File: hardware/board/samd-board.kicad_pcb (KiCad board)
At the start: 2 copper layers, 20.3 x 40.6 mm, 23 parts, among them J1 USB_B_Mini, J2 Conn_ARM_JTAG_SWD_10, J3 Conn_01x16_Male, J4 Conn_01x16_Male, SW1 SW_Push, U1 AZ1117-3.3, U2 ATSAMD21E17D-A, Y1 8MHz

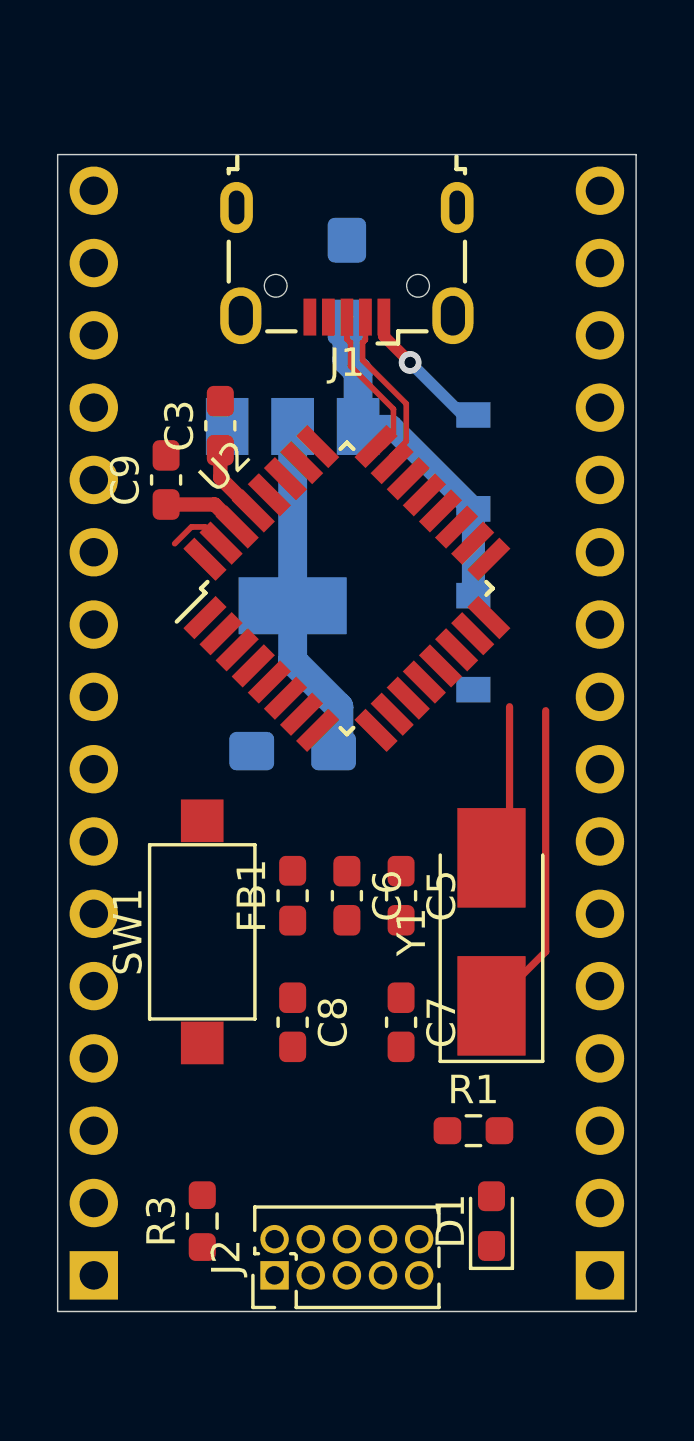
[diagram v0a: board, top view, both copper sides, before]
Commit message: complete basic routing
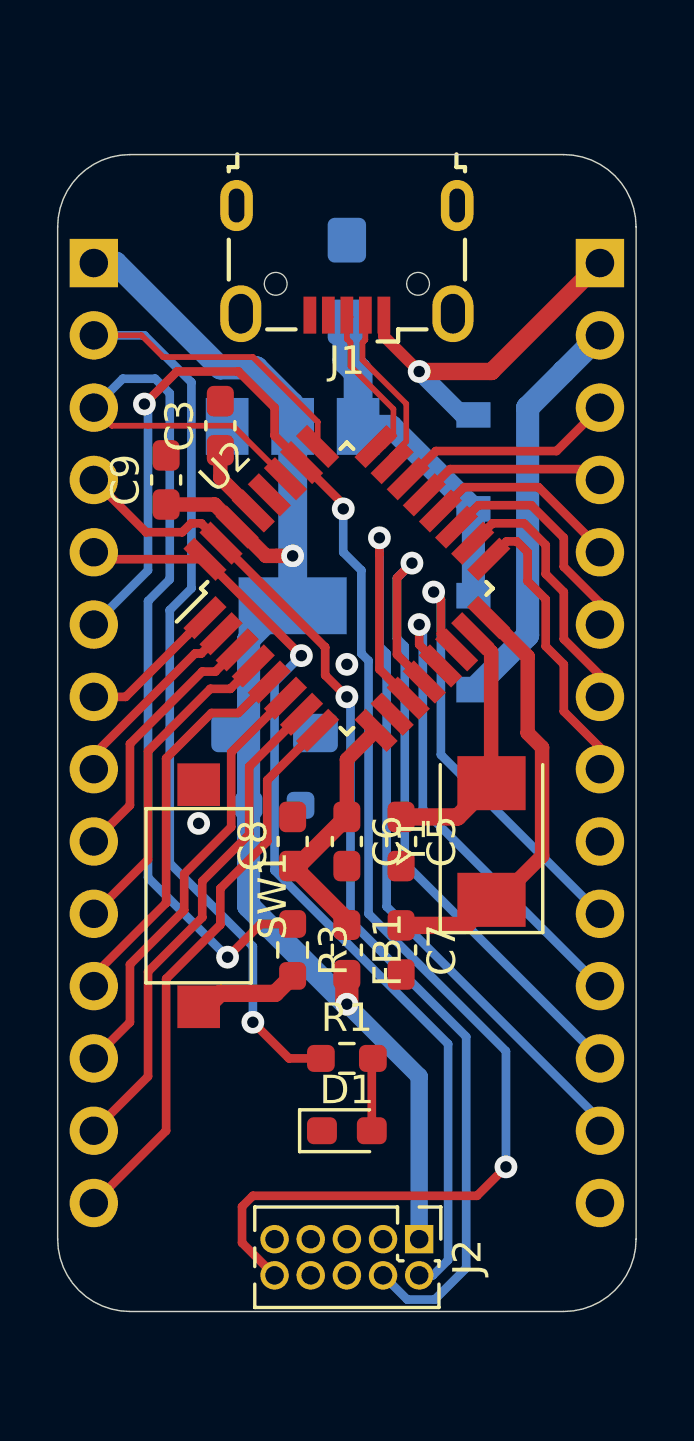
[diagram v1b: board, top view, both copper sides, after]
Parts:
- removed J3, J4: Conn_01x16_Male, Connector_PinHeader_2.54mm:PinHeader_1x16_P2.54mm_Vertical
- added J5: Conn_01x14_Male, Connector_PinHeader_2.54mm:PinHeader_1x14_P2.54mm_Vertical, B.Cu at (181.6, 83.8)
- added J6: Conn_01x14_Male, Connector_PinHeader_2.54mm:PinHeader_1x14_P2.54mm_Vertical, B.Cu at (199.4, 83.8)
- added R2: NP, Resistor_SMD:R_0603_1608Metric_Pad0.98x0.95mm_HandSolder, B.Cu at (188.0, 102.9)
- J1: footprint Connector_USB:USB_Micro-B_Wuerth_629105150521 -> Assorted:USB_Micro-B_Wuerth_629105150521
- Y1: footprint Crystal:Crystal_SMD_5032-2Pin_5.0x3.2mm_HandSoldering -> Assorted:Crystal_SMD_Abracon_ABM3-2Pin_5.0x3.2mm
- moved R3 10.0 mm to (188.6, 108.0), turned to 270 degrees
- moved C8 6.35 mm to (188.6, 104.1), turned to 90 degrees
- moved D1 5.99 mm to (190.5, 114.3), turned to 0 degrees
- moved J2 5.24 mm to (193.0, 118.1), turned to 270 degrees
- moved R1 5.12 mm to (190.5, 111.8)
- moved J1 3.82 mm to (190.5, 80.0)
- moved Y1 3.17 mm to (195.6, 104.1)
- moved FB1 2.69 mm to (190.5, 108.0), turned to 270 degrees
- moved C7 2.54 mm to (192.4, 108.0)
- moved C5 1.91 mm to (192.4, 104.1)
- moved C6 1.91 mm to (190.5, 104.1)
- moved SW1 1.28 mm to (185.3, 106.0), turned to 270 degrees
- moved C4 0.90 mm to (188.0, 100.3), turned to 0 degrees
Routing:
- net ~RESET: track 0.00 -> 56.9 mm, vias 0 -> 3
- net /PA27: track 0.00 -> 41.0 mm, vias 0 -> 1
- net SWCLK: track 2.81 -> 38.4 mm, vias 0 -> 1
- net /PA28: track 0.00 -> 34.7 mm, vias 0 -> 1
- net +3V3: track 14.9 -> 49.3 mm, vias 0 -> 2
- net SWDIO: track 0.00 -> 34.2 mm, vias 0 -> 1
- net /PA08: track 0.00 -> 30.1 mm, vias 0 -> 1
- net /PA09: track 0.00 -> 25.4 mm, vias 0 -> 1
- net /PA07: track 0.00 -> 19.9 mm
- net /PA06: track 0.00 -> 17.7 mm
- net /PA10: track 0.00 -> 17.1 mm, vias 0 -> 1
- net /PA11: track 0.00 -> 16.1 mm, vias 0 -> 1
- net /PA05: track 0.00 -> 15.4 mm
- net VDC: track 0.00 -> 14.3 mm
- net /PA04: track 0.00 -> 13.8 mm
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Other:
- outline, holes or cut-outs redrawn

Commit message: increase pin count from 28 to 32, complete routing
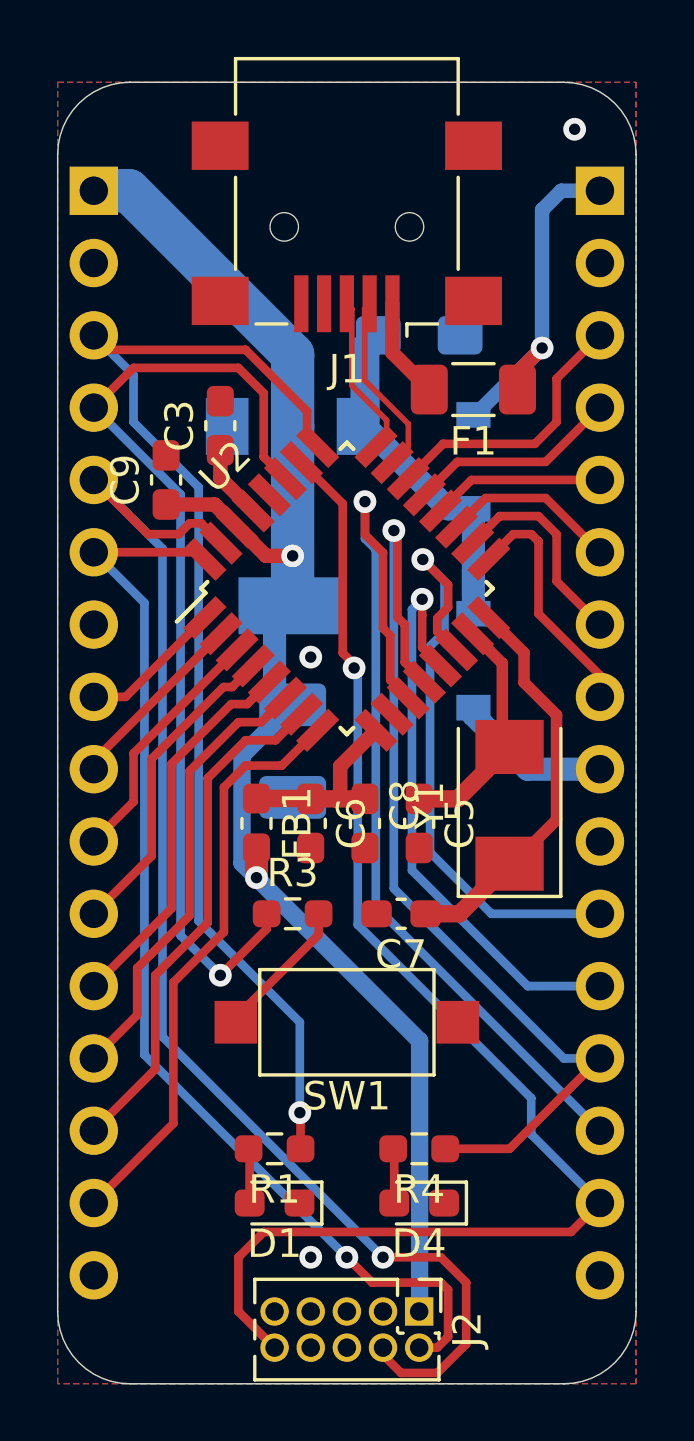
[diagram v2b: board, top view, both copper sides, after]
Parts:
- removed J5, J6: Conn_01x14_Male, Connector_PinHeader_2.54mm:PinHeader_1x14_P2.54mm_Vertical
- removed R2: NP, Resistor_SMD:R_0603_1608Metric_Pad0.98x0.95mm_HandSolder
- added D4: LED, LED_SMD:LED_0603_1608Metric_Pad1.05x0.95mm_HandSolder, F.Cu at (193.0, 116.8)
- added F1: Polyfuse, Resistor_SMD:R_1206_3216Metric_Pad1.30x1.75mm_HandSolder, F.Cu at (194.9, 88.3)
- added J3: Conn_01x16_Male, Connector_PinHeader_2.54mm:PinHeader_1x16_P2.54mm_Vertical, B.Cu at (181.6, 81.3)
- added J4: Conn_01x16_Male, Connector_PinHeader_2.54mm:PinHeader_1x16_P2.54mm_Vertical, B.Cu at (199.4, 81.3)
- added R4: 1k5, Resistor_SMD:R_0603_1608Metric_Pad0.98x0.95mm_HandSolder, F.Cu at (193.0, 114.9)
- C4: footprint Capacitor_Tantalum_SMD:CP_EIA-3216-18_Kemet-A_Pad1.58x1.35mm_HandSolder -> Capacitor_Tantalum_SMD:CP_EIA-3528-21_Kemet-B_Pad1.50x2.35mm_HandSolder
- J1: footprint Assorted:USB_Micro-B_Wuerth_629105150521 -> Connector_USB:USB_Mini-B_Lumberg_2486_01_Horizontal
- moved SW1 6.85 mm to (190.5, 110.5), turned to 180 degrees
- moved FB1 5.46 mm to (187.3, 103.5)
- moved R1 4.07 mm to (188.0, 114.9), turned to 180 degrees
- moved D1 3.59 mm to (188.0, 116.8), turned to 180 degrees
- moved C2 3.17 mm to (193.0, 86.4), turned to 0 degrees
- moved C8 2.62 mm to (191.1, 103.5), turned to 270 degrees
- moved J1 2.55 mm to (190.5, 82.5)
- moved J2 2.54 mm to (193.0, 120.7)
- moved C6 1.42 mm to (189.2, 103.5)
- moved Y1 1.42 mm to (196.2, 102.9)
- moved C7 1.27 mm to (192.4, 106.7), turned to 180 degrees
- moved R3 1.27 mm to (188.6, 106.7), turned to 0 degrees
- moved C4 0.90 mm to (188.6, 101.0), turned to 270 degrees
- moved C5 0.90 mm to (193.0, 103.5)
- moved D2 0.64 mm to (194.9, 97.8)
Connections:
- J1 pad 1: VBUS -> Net-(F1-Pad2)
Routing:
- net /PA09: track 25.4 -> 34.8 mm
- net ~RESET: track 56.9 -> 47.5 mm, vias 3 -> 1
- net VDC: track 14.3 -> 5.49 mm
- net SWCLK: track 38.4 -> 46.5 mm
- net /PA11: track 16.1 -> 21.7 mm
- net SWDIO: track 34.2 -> 39.3 mm
- net +3V3: track 49.3 -> 53.5 mm
- net Net-(F1-Pad2): track 0.00 -> 3.55 mm
- net /PA10: track 17.1 -> 20.6 mm
- net /PA08: track 30.1 -> 33.0 mm
- net +3.3VA: track 8.95 -> 6.82 mm
- net /PA23: track 7.77 -> 9.71 mm
- net Net-(D4-Pad2): track 0.00 -> 1.92 mm
- net /PA17: track 9.29 -> 7.41 mm
- net /PA18: track 8.13 -> 6.25 mm
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- added copper zone on B.Cu, net GND
- added copper zone on F.Cu, net GND
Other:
- board size 20.3 x 40.6 mm -> 20.3 x 45.7 mm

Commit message: complete component silkscreen placement
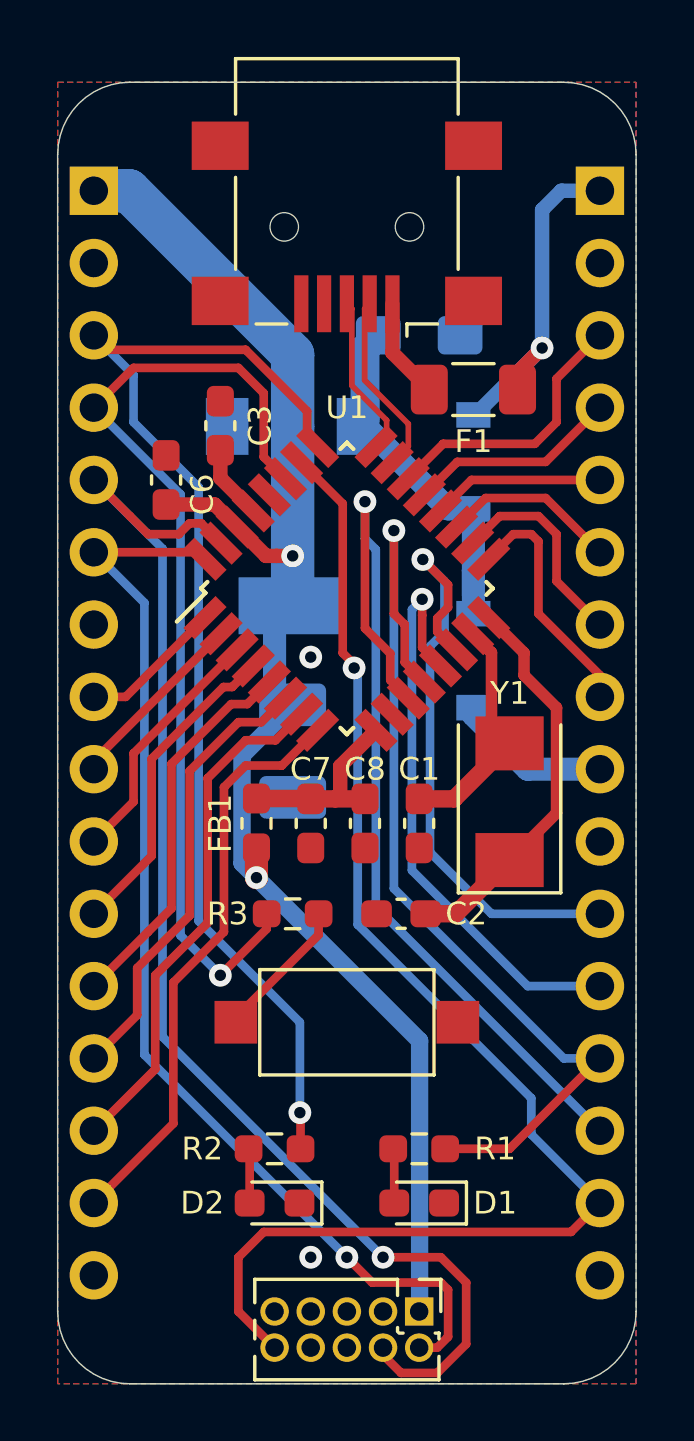
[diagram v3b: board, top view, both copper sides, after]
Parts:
- removed the C4 at (188.6, 101.0)
- removed the D2 at (194.9, 97.8)
- added C5: 47u 10V, Capacitor_Tantalum_SMD:CP_EIA-3528-21_Kemet-B_Pad1.50x2.35mm_HandSolder, B.Cu at (188.6, 101.0)
- added D4: D_Schottky, Diode_SMD:D_SOD-123, B.Cu at (194.9, 90.8)
- C4: renamed from C2; value 10u 10V -> 10u 16V
- moved D3 6.98 mm to (194.9, 97.8), turned to 270 degrees
- moved Y1 0.13 mm to (196.2, 102.7)
- renumbered C5 to C1, C7 to C2, C9 to C6, C6 to C7, D4 to D1, D1 to D2, R4 to R1, R1 to R2, U2 to U1, U1 to U2
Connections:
- D3 pad 2: VBUS -> VDC
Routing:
- net GND: vias 3 -> 2

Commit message: add power LED, pin silkscreen markers
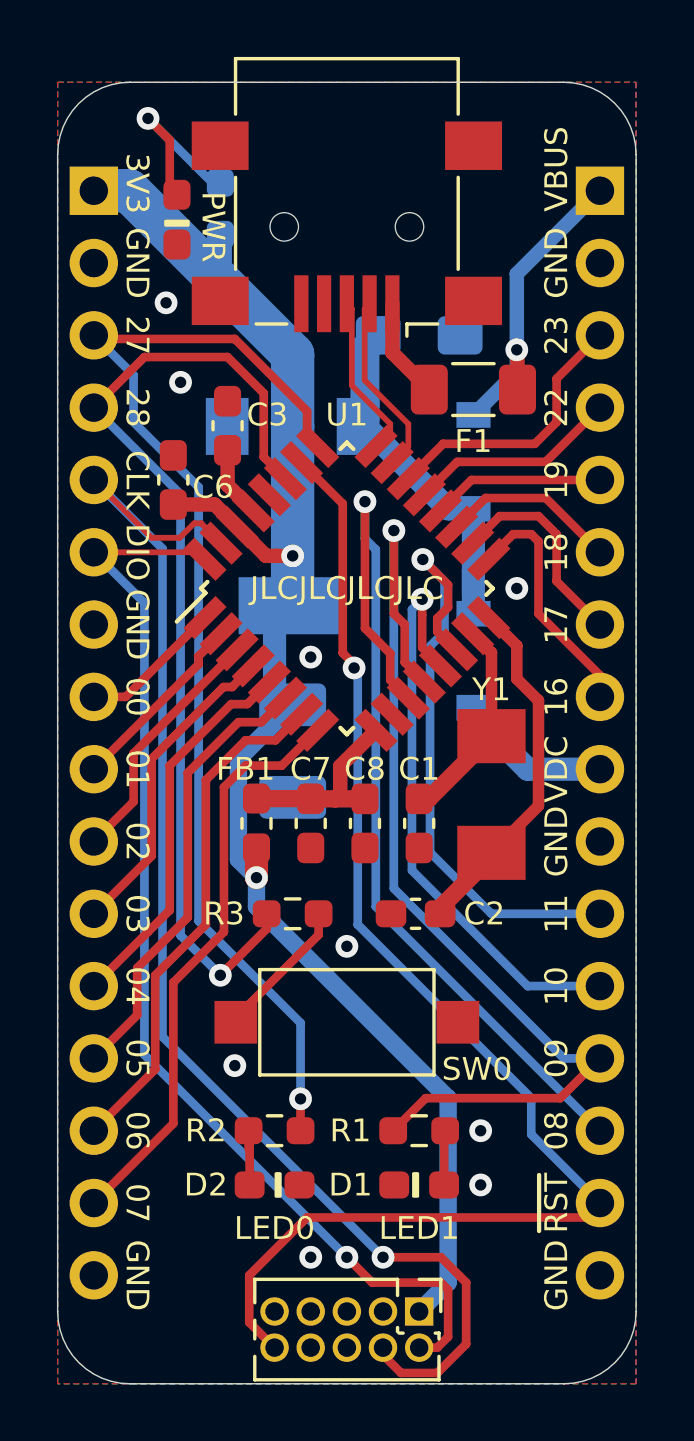
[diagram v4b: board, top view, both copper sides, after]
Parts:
- added D5: LED, Assorted:LED_0603_1608Metric_Pad1.05x0.95mm_HandSolder, F.Cu at (184.5, 82.3)
- added R4: 1k5, Resistor_SMD:R_0603_1608Metric_Pad0.98x0.95mm_HandSolder, B.Cu at (186.1, 81.9)
- D1, D2: footprint LED_SMD:LED_0603_1608Metric_Pad1.05x0.95mm_HandSolder -> Assorted:LED_0603_1608Metric_Pad1.05x0.95mm_HandSolder
- moved Y1 0.68 mm to (195.6, 102.5)
- moved D1 0.64 mm to (193.0, 116.2), turned to 0 degrees
- moved D2 0.64 mm to (188.0, 116.2)
- moved R1 0.64 mm to (193.0, 114.3), turned to 0 degrees
- moved R2 0.64 mm to (188.0, 114.3)
- moved C2 0.51 mm to (192.9, 106.7)
- moved C3 0.25 mm to (186.3, 89.5)
- moved C6 0.25 mm to (184.4, 91.4)
- renumbered SW1 to SW0
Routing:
- net Net-(D5-Pad2): track 0.00 -> 6.58 mm, vias 0 -> 1
- net +3V3: track 53.5 -> 56.7 mm
- net Net-(C2-Pad1): track 14.0 -> 12.0 mm
- net /PA09: track 34.8 -> 36.4 mm
- net VBUS: track 12.4 -> 11.1 mm
- net ~RESET: track 47.5 -> 46.6 mm
- net /PA27: track 41.6 -> 40.9 mm
- net Net-(D2-Pad2): track 1.92 -> 2.56 mm
- net GND: track 0.00 -> 0.05 mm, vias 2 -> 9
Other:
- board text added: "00"
- board text added: "01"
- board text added: "02"
- board text added: "03"
- board text added: "04"
- board text added: "05"
- board text added: "06"
- board text added: "07"
- board text added: "08"
- board text added: "09"
- board text added: "10"
- board text added: "11"
- board text added: "16"
- board text added: "17"
- board text added: "18"
- board text added: "19"
- board text added: "22"
- board text added: "23"
- board text added: "27"
- board text added: "28"
- board text added: "3V3"
- board text added: "CLK"
- board text added: "DIO"
- board text added: "GND"
- board text added: "JLCJLCJLCJLC"
- board text added: "LED0"
- board text added: "LED1"
- board text added: "PWR"
- board text added: "VBUS"
- board text added: "VDC"
- board text added: "~RST"

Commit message: complete board
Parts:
- removed N1: Housing, Assorted:Template_Breadboard
- moved R4 3.86 mm to (186.7, 85.7), turned to 180 degrees
- moved D5 0.18 mm to (184.4, 82.4), turned to 270 degrees
- moved Y1 0.13 mm to (195.7, 102.5)
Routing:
- net Net-(D5-Pad2): track 6.58 -> 3.79 mm
- net +3V3: track 56.7 -> 55.6 mm
- net GND: vias 9 -> 8
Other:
- board text added: "1"
- board text added: "30"
- board text added: "31"
- board text added: "SAMD21-dev"
- board text added: "SWD"
- board text removed: "CLK"
- board text removed: "DIO"
